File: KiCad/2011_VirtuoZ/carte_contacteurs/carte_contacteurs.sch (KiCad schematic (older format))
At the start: 11 parts, among them P1 CONN_1, P5 CONN_1, P6 CONN_1, P7 CONN_1, U1 REED9081_SYMBIOZ, U2 REED9081_SYMBIOZ

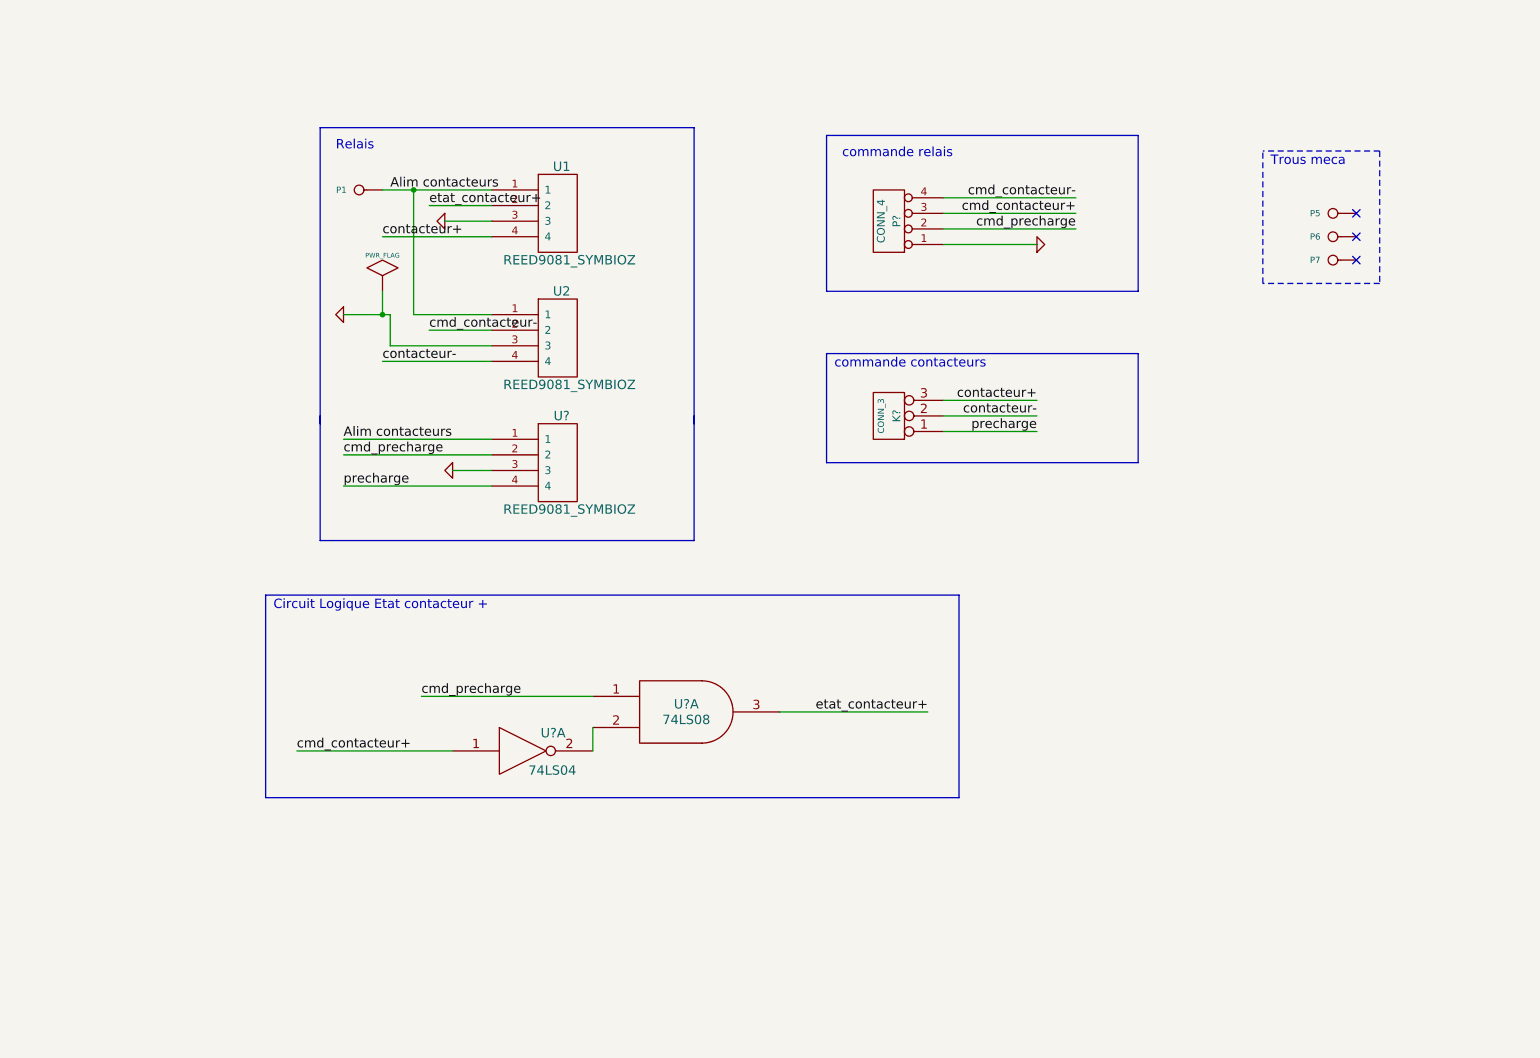
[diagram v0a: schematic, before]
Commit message: correction circuit logique
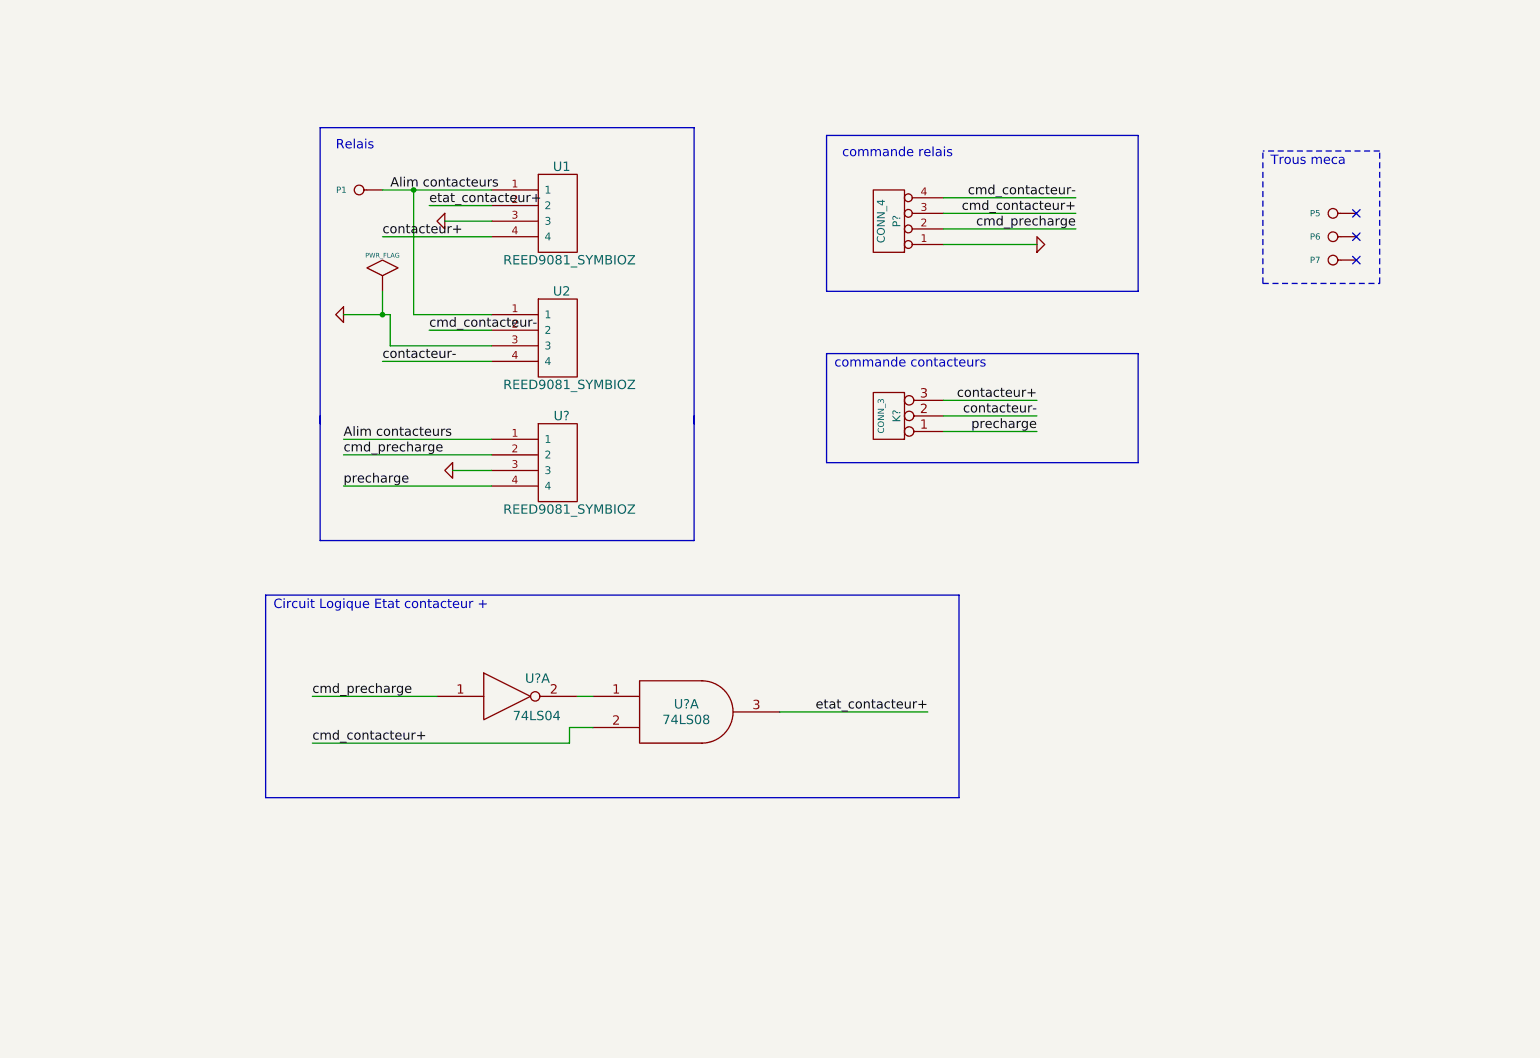
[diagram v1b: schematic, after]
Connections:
- net cmd_contacteur+: now also U?.2; no longer U?.1
- net cmd_precharge: now also U?.1; no longer U?.1
- net at U?.2: now also U?.1; no longer U?.2
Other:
- moved on the sheet: U?A
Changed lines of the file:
@@
-EESchema Schematic File Version 2  date ven. 04 mars 2011 18:02:25 CET
+EESchema Schematic File Version 2  date 17/03/2011 18:39:53
 LIBS:power
 LIBS:device
@@
 Sheet 1 1
 Title ""
-Date "4 mar 2011"
+Date "17 mar 2011"
 Rev ""
 Comp ""
@@
 Comment4 ""
 $EndDescr
-Text Notes 2350 4350 0    60   ~ 0
-Circuit Logique Etat contacteur +\n
+Wire Wire Line
+	4250 5100 4400 5100
+Wire Wire Line
+	4250 5200 4250 5100
+Wire Wire Line
+	2600 5200 4250 5200
+Wire Wire Line
+	4300 4900 4400 4900
 Wire Bus Line
-	2300 5550 2300 4250
+	2650 3100 2650 3900
 Wire Bus Line
-	2300 5550 6750 5550
+	2650 3900 5050 3900
 Wire Bus Line
-	6750 5550 6750 4250
+	5050 3900 5050 3100
+Wire Wire Line
+	3750 3350 2800 3350
+Wire Wire Line
+	2800 3250 3750 3250
+Wire Wire Line
+	6650 1700 7500 1700
+Connection ~ 3050 2450
+Wire Wire Line
+	3050 2300 3050 2450
 Wire Bus Line
-	6750 4250 2300 4250
+	5900 3400 5900 2700
+Wire Bus Line
+	5900 3400 7900 3400
+Wire Bus Line
+	7900 3400 7900 2700
+Wire Bus Line
+	7900 2700 5900 2700
 Wire Wire Line
-	5600 5000 6550 5000
+	6650 3100 7250 3100
 Wire Wire Line
-	4400 4900 3300 4900
+	6650 2000 7250 2000
+Wire Wire Line
+	6650 1800 7500 1800
+Wire Wire Line
+	3350 1750 3750 1750
+Wire Wire Line
+	3750 1950 3050 1950
+Wire Wire Line
+	3750 1650 3250 1650
+Wire Wire Line
+	3250 1650 3050 1650
+Wire Wire Line
+	3250 1650 3250 2450
+Wire Wire Line
+	3250 2450 3750 2450
+Connection ~ 3250 1650
+Wire Wire Line
+	3750 2750 3050 2750
+Wire Wire Line
+	3750 2550 3350 2550
+Wire Wire Line
+	6650 3000 7250 3000
+Wire Wire Line
+	3750 1850 3450 1850
+Wire Bus Line
+	5900 2300 5900 1300
+Wire Bus Line
+	5900 2300 7900 2300
+Wire Bus Line
+	7900 2300 7900 1300
+Wire Bus Line
+	7900 1300 5900 1300
+Wire Bus Line
+	5050 1250 2650 1250
+Wire Bus Line
+	5050 1250 5050 3150
+Wire Bus Line
+	2650 1250 2650 3150
+Wire Wire Line
+	3750 2650 3100 2650
+Wire Wire Line
+	3100 2650 3100 2450
+Wire Wire Line
+	3100 2450 3050 2450
+Wire Wire Line
+	3050 2450 2800 2450
+Wire Notes Line
+	8700 2250 8700 1400
+Wire Notes Line
+	8700 2250 9450 2250
+Wire Notes Line
+	9450 2250 9450 1400
+Wire Notes Line
+	9450 1400 8700 1400
+Wire Wire Line
+	6650 1900 7500 1900
+Wire Wire Line
+	6650 3200 7250 3200
+Wire Wire Line
+	3750 3550 2800 3550
 Wire Wire Line
 	3750 3450 3500 3450
 Wire Wire Line
-	3750 3550 2800 3550
+	5600 5000 6550 5000
+Wire Bus Line
+	6750 4250 2300 4250
+Wire Bus Line
+	6750 4250 6750 5550
+Wire Bus Line
+	6750 5550 2300 5550
+Wire Bus Line
+	2300 5550 2300 4250
 Wire Wire Line
-	6650 3200 7250 3200
-Wire Wire Line
-	6650 1900 7500 1900
-Wire Notes Line
-	9450 1400 8700 1400
-Wire Notes Line
-	9450 1400 9450 2250
-Wire Notes Line
-	9450 2250 8700 2250
-Wire Notes Line
-	8700 2250 8700 1400
-Wire Wire Line
-	2800 2450 3100 2450
-Wire Wire Line
-	3100 2450 3100 2650
-Wire Wire Line
-	3100 2650 3750 2650
-Wire Bus Line
-	2650 3150 2650 1250
-Wire Bus Line
-	5050 3150 5050 1250
-Wire Bus Line
-	5050 1250 2650 1250
-Wire Bus Line
-	7900 1300 5900 1300
-Wire Bus Line
-	7900 1300 7900 2300
-Wire Bus Line
-	7900 2300 5900 2300
-Wire Bus Line
-	5900 2300 5900 1300
-Wire Wire Line
-	3750 1850 3450 1850
-Wire Wire Line
-	6650 3000 7250 3000
-Wire Wire Line
-	3750 2550 3350 2550
-Wire Wire Line
-	3750 2750 3050 2750
-Connection ~ 3250 1650
-Wire Wire Line
-	3750 2450 3250 2450
-Wire Wire Line
-	3250 2450 3250 1650
-Wire Wire Line
-	3750 1650 3050 1650
-Wire Wire Line
-	3750 1950 3050 1950
-Wire Wire Line
-	3350 1750 3750 1750
-Wire Wire Line
-	6650 1800 7500 1800
-Wire Wire Line
-	6650 2000 7250 2000
-Wire Wire Line
-	6650 3100 7250 3100
-Wire Bus Line
-	7900 2700 5900 2700
-Wire Bus Line
-	7900 2700 7900 3400
-Wire Bus Line
-	7900 3400 5900 3400
-Wire Bus Line
-	5900 3400 5900 2700
-Wire Wire Line
-	3050 2300 3050 2450
-Connection ~ 3050 2450
-Wire Wire Line
-	6650 1700 7500 1700
-Wire Wire Line
-	2800 3250 3750 3250
-Wire Wire Line
-	3750 3350 2800 3350
-Wire Wire Line
-	4400 5250 4400 5100
-Wire Wire Line
-	3500 5250 2500 5250
-Wire Bus Line
-	5050 3100 5050 3900
-Wire Bus Line
-	5050 3900 2650 3900
-Wire Bus Line
-	2650 3900 2650 3100
+	2600 4900 3400 4900
+Text Notes 2350 4350 0    60   ~ 0
+Circuit Logique Etat contacteur +\n
 Text Label 6550 5000 2    60   ~ 0
 etat_contacteur+
-Text Label 2500 5250 0    60   ~ 0
+Text Label 2600 5200 0    60   ~ 0
 cmd_contacteur+
-Text Label 3300 4900 0    60   ~ 0
+Text Label 2600 4900 0    60   ~ 0
 cmd_precharge
 $Comp
@@
 L 74LS04 U?
 U 1 1 4D711A74
-P 3950 5250
-F 0 "U?" H 4145 5365 60  0000 C CNN
-F 1 "74LS04" H 4140 5125 60  0000 C CNN
-	1    3950 5250
+P 3850 4900
+F 0 "U?" H 4045 5015 60  0000 C CNN
+F 1 "74LS04" H 4040 4775 60  0000 C CNN
+	1    3850 4900
 	1    0    0    -1
 $EndComp

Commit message: 
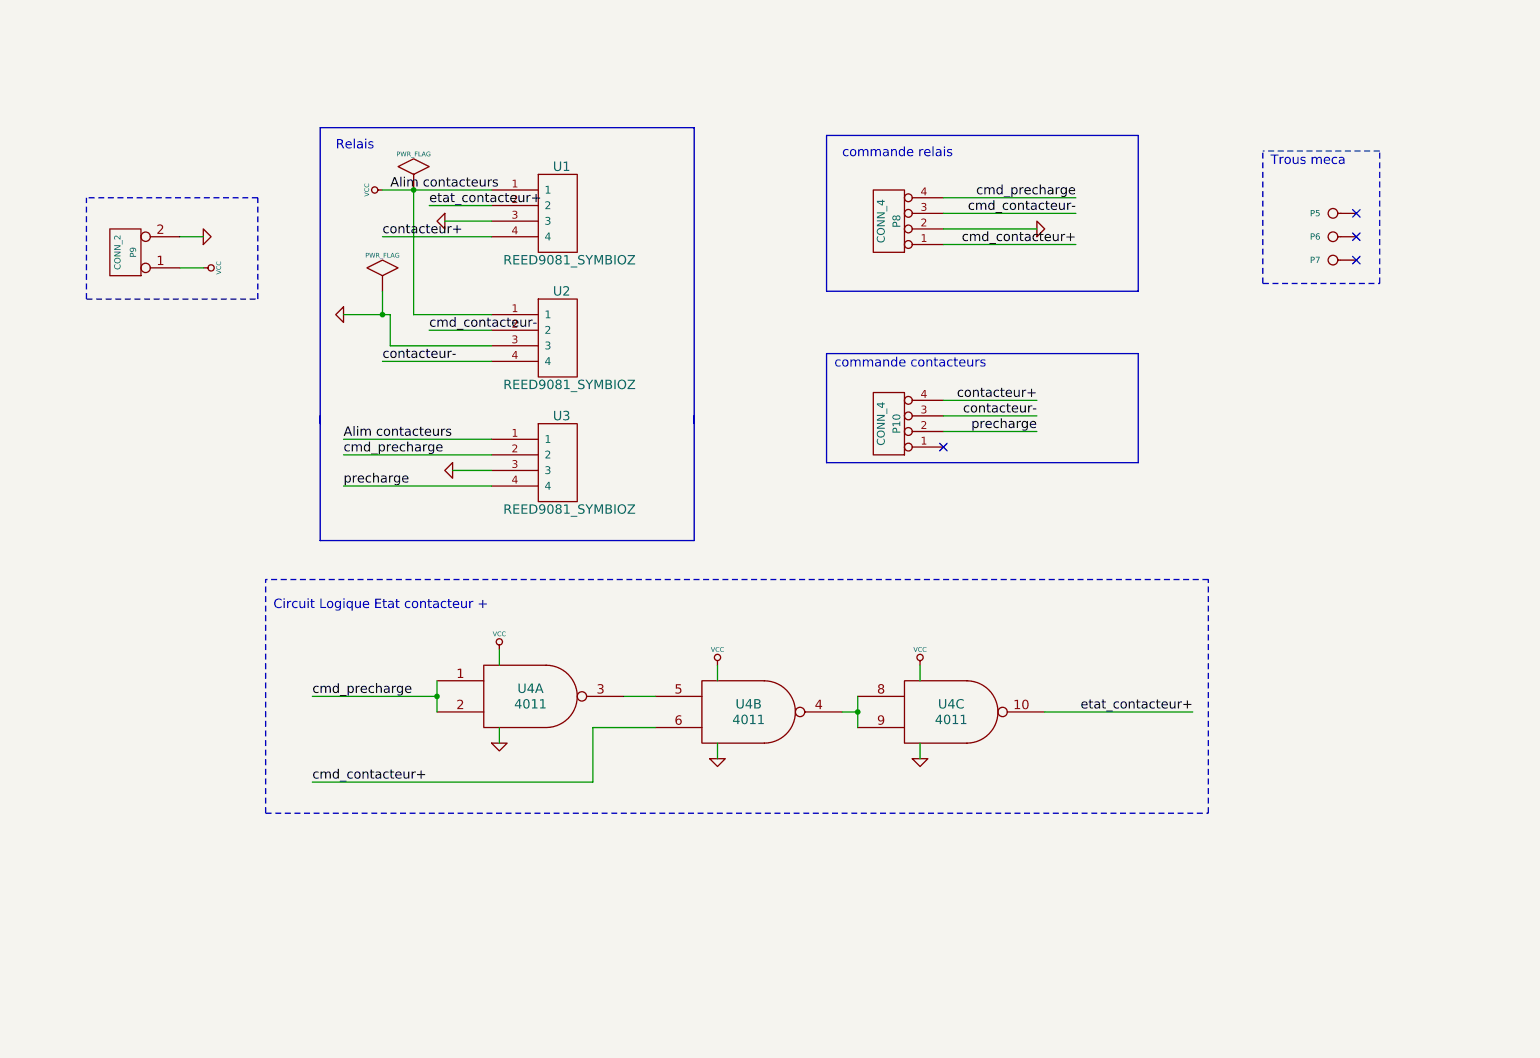
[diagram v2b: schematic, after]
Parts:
- removed K?: CONN_3, symbol CONN_3
- removed P1: CONN_1, symbol CONN_1
- removed U?: 74LS04, symbol 74LS04
- removed U?: 74LS08, symbol 74LS08
- added P10: CONN_4, symbol CONN_4
- added P9: CONN_2, symbol CONN_2
- added U4: 4011, symbol 4011
- gave numbers to parts that had none: 2
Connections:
- net Alim contacteurs is gone; now on net VCC: U1.1, U2.1, U3.1
- net GND: now also P8.2 (P2), P9.2 (PM), U4.7 (VSS), U4.7 (VSS), U4.7 (VSS); no longer P8.1 (P1)
- net VCC: now also P9.1 (P1), U4.14 (VDD), U4.14 (VDD), U4.14 (VDD)
- net cmd_contacteur+: now also P8.1 (P1), U4.6; no longer P8.3 (P3)
- net cmd_contacteur-: now also P8.3 (P3); no longer P8.4 (P4)
- net cmd_precharge: now also P8.4 (P4), U4.1, U4.2; no longer P8.2 (P2)
- net contacteur+: now also P10.4 (P4)
- net contacteur-: now also P10.3 (P3)
- net etat_contacteur+: now also U4.10
- net precharge: now also P10.2 (P2)
- new net: U4.3, U4.5
- new net: U4.4, U4.8, U4.9
- no-connect marks 3 -> 4

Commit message: Validation carte contacteurs v1.0
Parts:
- removed U2: REED9081_SYMBIOZ, symbol REED9081_SYMBIOZ
- added C1: 10u, symbol CP
- added C2, C4: 27p, symbol C
- added C3: 1u, symbol CP
- added MECA4: MECA, symbol CONN_1
- added U2: LM7805, symbol LM7805
- added U3: REED9081_SYMBIOZ, symbol REED9081_SYMBIOZ
- MECA1: renamed from P5; value CONN_1 -> MECA
- MECA2: renamed from P6; value CONN_1 -> MECA
- MECA3: renamed from P7; value CONN_1 -> MECA
- P1: renamed from P8; value CONN_4 -> INTERFACE
- P2: renamed from P9; value CONN_2 -> ALIM
- P3: renamed from P10; value CONN_4 -> CONTACT.
- renumbered U3 to U4, U4 to U5
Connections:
- net labels added: +12P, +12V, cmd_secu_cont+
- net labels removed: Alim contacteurs, etat_contacteur+
- wire segments 40 -> 50
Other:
- note added: "Alim"
- note added: "Commande contacteurs"
- note added: "Contacteurs"
- note removed: "commande contacteurs"
- note removed: "commande relais"
- moved on the sheet: MECA1, MECA2, MECA3, P1, P2, P3, U4

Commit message: validation carte contacteurs
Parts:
- removed U5: 4011, symbol 4011
- added Q1, Q2, Q3: FET_N, symbol FET_N
- added U5: 4001, symbol 4001
- renumbered P2 to P1, P1 to P2, U2 to U1, U1 to U2
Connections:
- wire segments 50 -> 69
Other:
- moved on the sheet: MECA1, MECA2, MECA3, MECA4, P1, P2, P3, U2, U3, U4

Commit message: Remplacement relais
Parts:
- removed C3: 1u, symbol CP
- removed C4: 27p, symbol C
- removed U2, U3: REED9081_SYMBIOZ, symbol REED9081_SYMBIOZ
- added K1, K2: RELAIS-DPDT, symbol RELAIS-DPDT
- added R1, R2: 2K, symbol R
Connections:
- wire segments 69 -> 63
- no-connect marks 4 -> 12
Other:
- note added: "Relais contacteur +\n"
- note added: "Relais contacteur -\n"
- note removed: "Relais\n"
- moved on the sheet: MECA1, MECA2, MECA3, MECA4, P1, P2, P3, U4
